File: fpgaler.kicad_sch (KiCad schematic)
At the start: 21 parts, among them J3 USB_C_Receptacle_USB2.0, J4 MicroSd, J5 JST

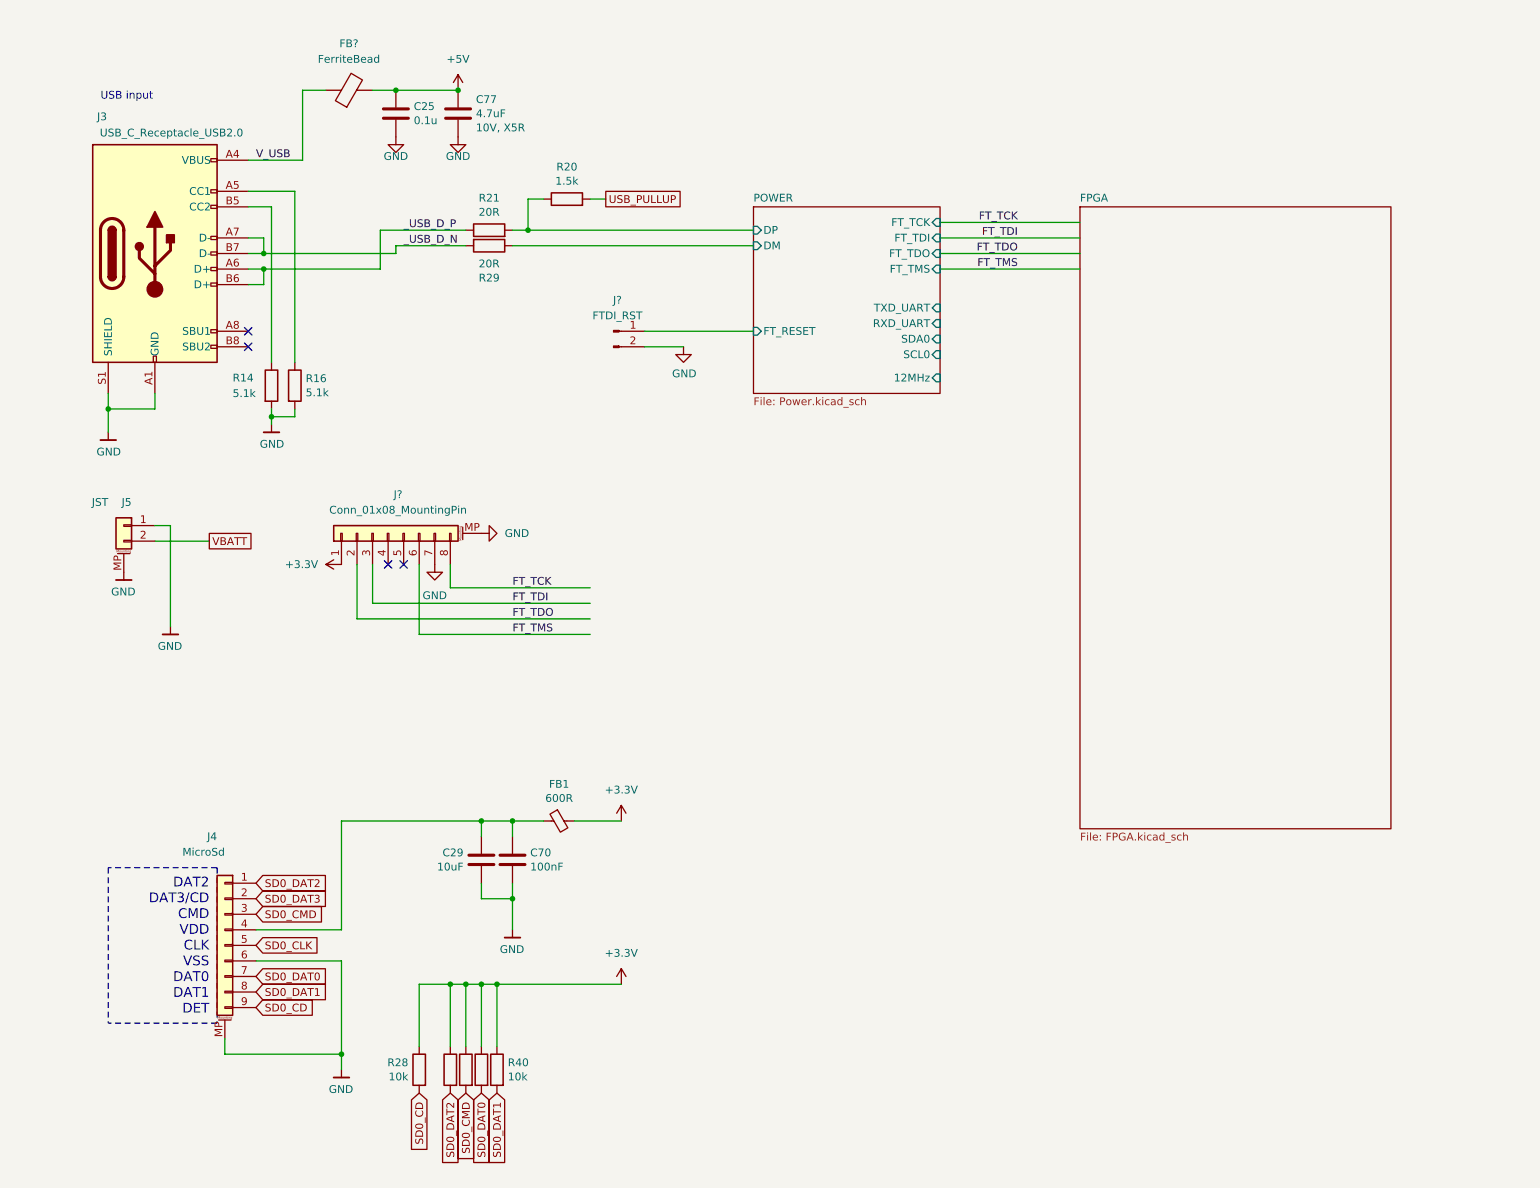
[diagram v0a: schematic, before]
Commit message: split fpga into two sheet. Connect jtag signals.
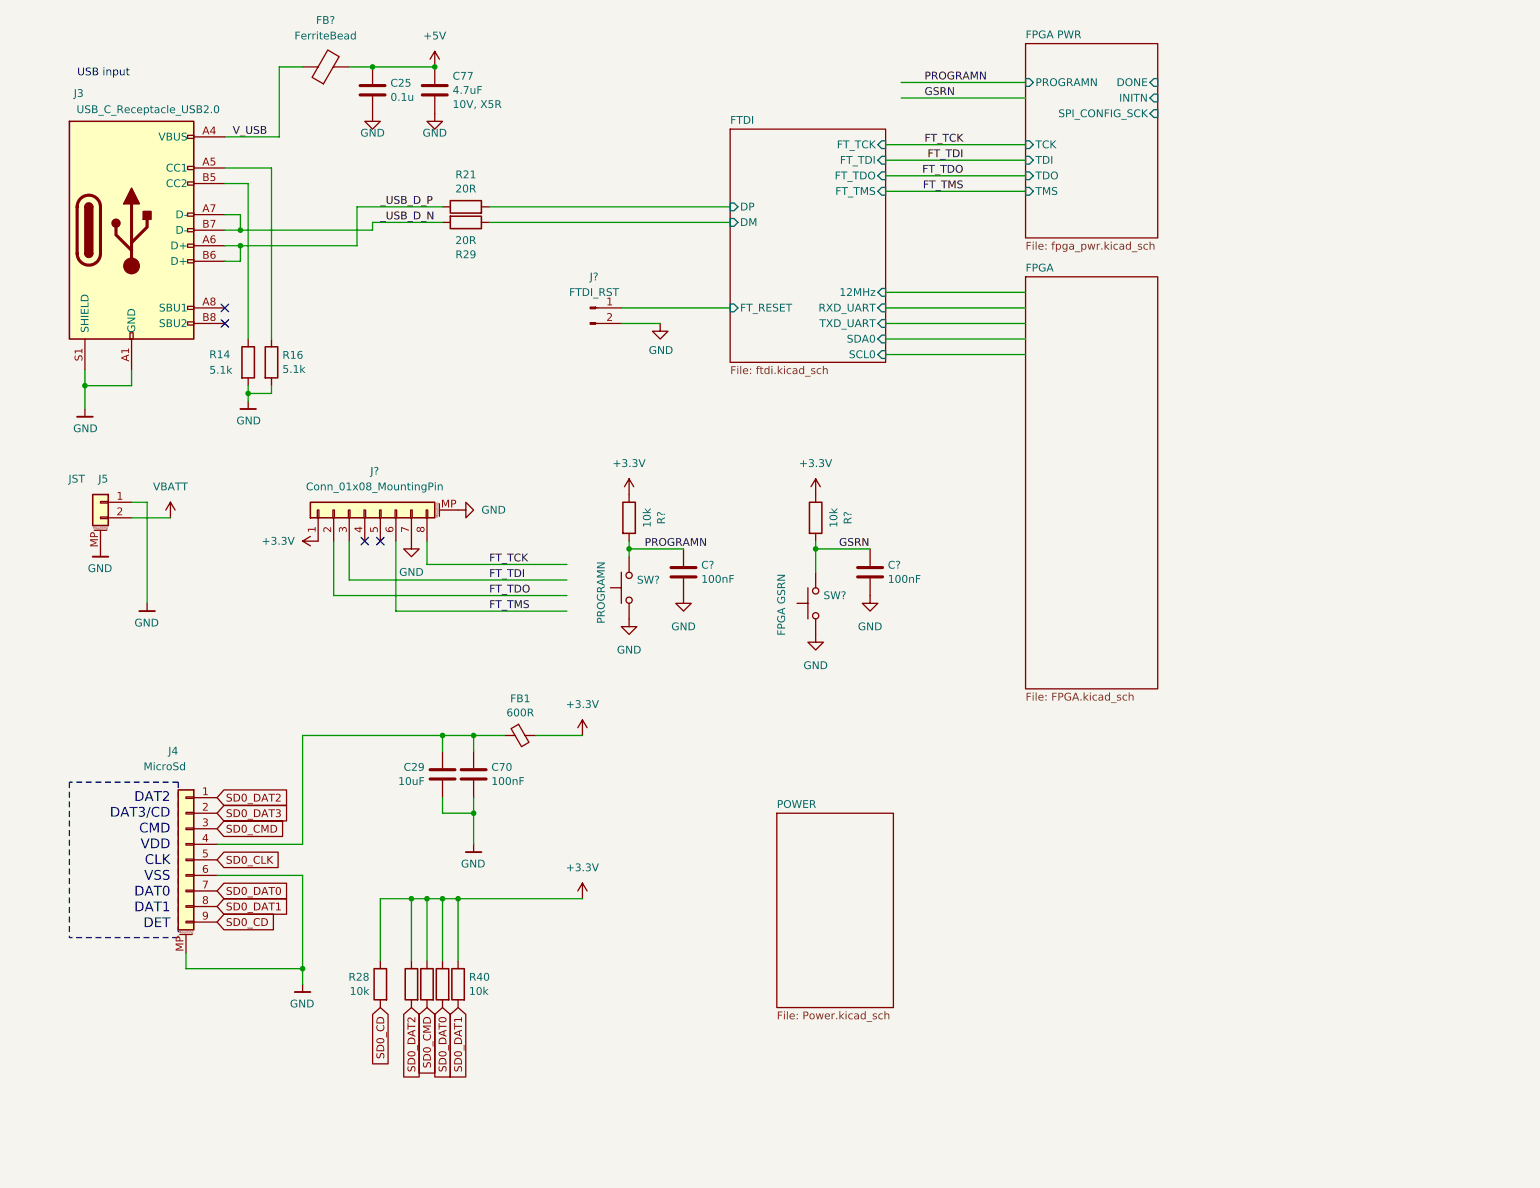
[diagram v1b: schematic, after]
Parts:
- removed R20: 1.5k, gkl_dipol:R_0201_0603Metric, symbol Device:R
- added C? (x2): 100nF, gkl_dipol:C_0201_0603Metric, symbol Device:C
- added R? (x2): 10k, gkl_dipol:R_0201_0603Metric, symbol Device:R
- added SW?: PROGRAMN, symbol Switch:SW_Push
- added SW?: FPGA GSRN, symbol Switch:SW_Push
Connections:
- net +3.3V: now also R?.1, R?.1
- net GND: now also C?.1, C?.1, SW?.1, SW?.1
- net POWER/DM renamed FTDI/DM
- net POWER/DP renamed FTDI/DP
- net POWER/FT_RESET renamed FTDI/FT_RESET
- new net GSRN: C?.2, R?.2, SW?.2
- new net PROGRAMN: C?.2, R?.2, SW?.2
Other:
- added sheet FPGA PWR (fpga_pwr.kicad_sch)
- added sheet FTDI (ftdi.kicad_sch)
- sheet POWER ports: added none; removed 12MHz, DM, DP, FT_RESET, FT_TCK, FT_TDI, FT_TDO, FT_TMS, RXD_UART, SCL0, SDA0, TXD_UART
- title: (none) -> FPGALER 
- moved on the sheet: C25, C29, C70, C77, FB1, FB?, J3, J4, J5, J?, R14, R16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

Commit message: complete scheme, add rotary switch, leds and buttons
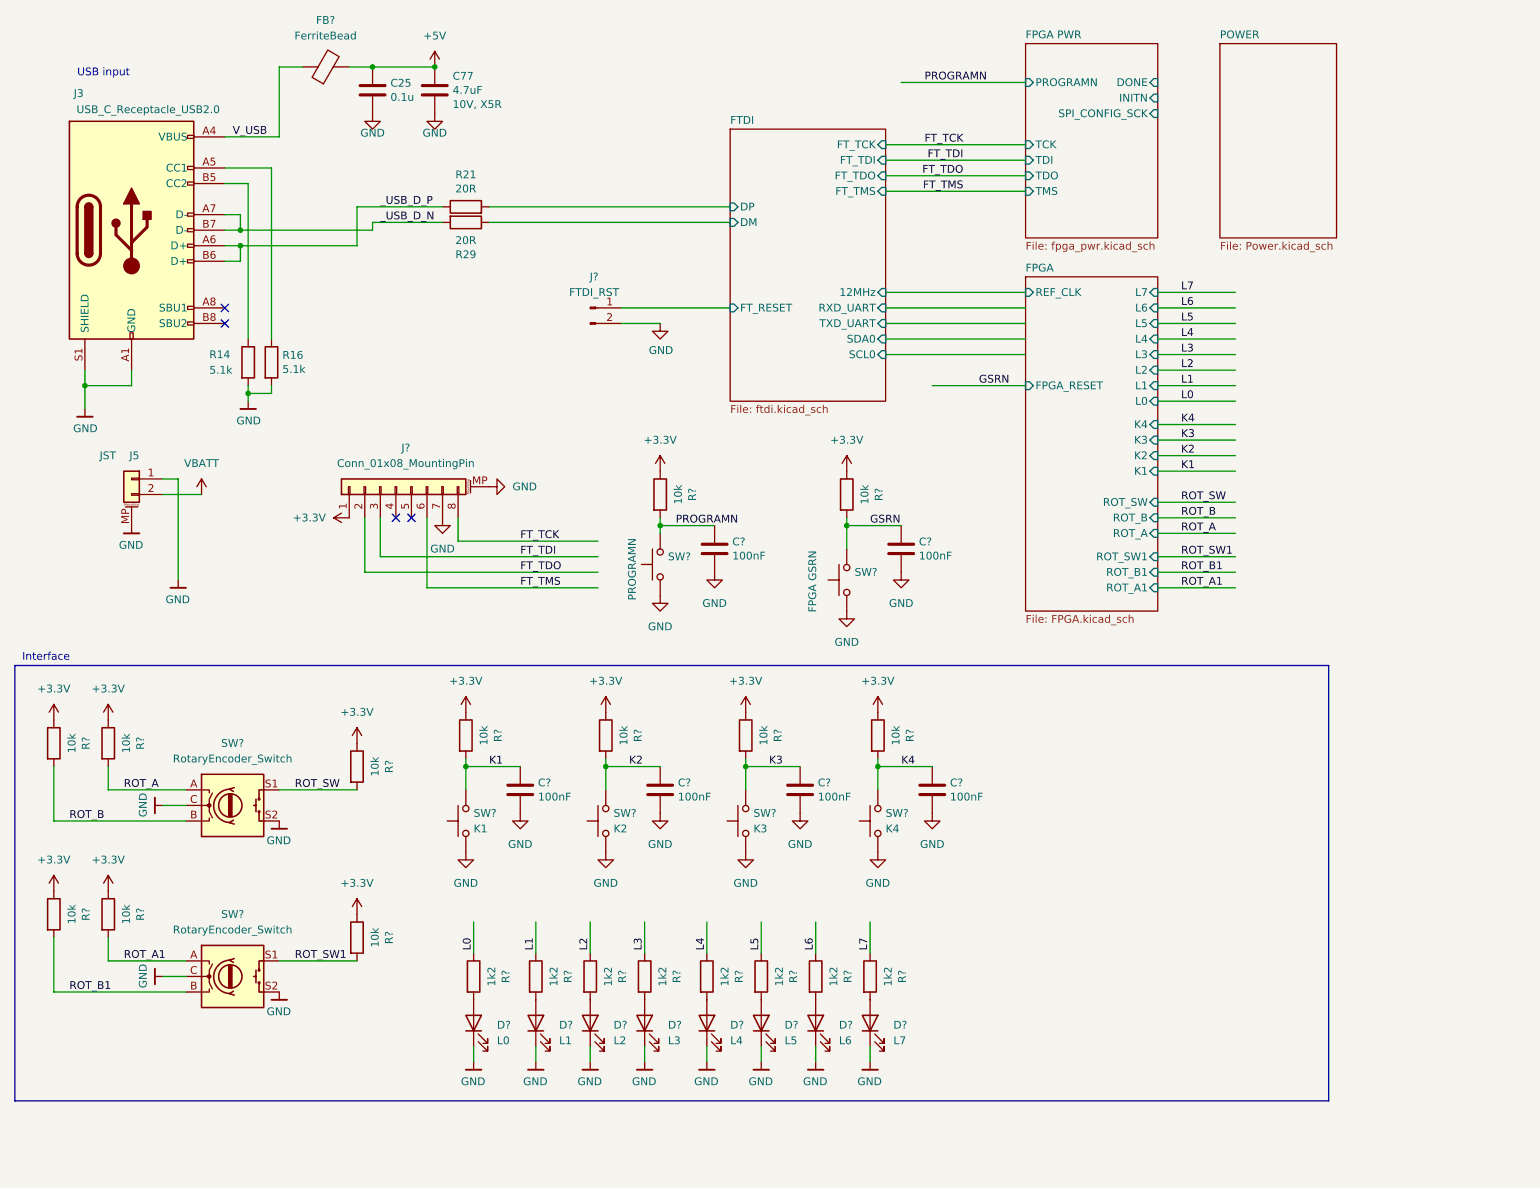
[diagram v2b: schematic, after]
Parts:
- removed C29: 10uF, Capacitor_SMD:C_0402_1005Metric, symbol Device:C
- removed C70: 100nF, gkl_dipol:C_0201_0603Metric, symbol Device:C
- removed FB1: 600R, Inductor_SMD:L_0402_1005Metric, symbol Device:Ferrite_Bead_Small
- removed J4: MicroSd, gkl_conn:molex_microsd_1040310811, symbol Connector_Generic_MountingPin:Conn_01x09_MountingPin
- removed R28, R40, R41, R42, R43: 10k, gkl_dipol:R_0201_0603Metric, symbol Device:R
- added C? (x4): 100nF, gkl_dipol:C_0201_0603Metric, symbol Device:C
- added D?: L3, symbol Device:LED
- added D?: L4, symbol Device:LED
- added D?: L0, symbol Device:LED
- added D?: L7, symbol Device:LED
- added D?: L6, symbol Device:LED
- added D?: L2, symbol Device:LED
- added D?: L1, symbol Device:LED
- added D?: L5, symbol Device:LED
- added R? (x10): 10k, gkl_dipol:R_0201_0603Metric, symbol Device:R
- added R? (x8): 1k2, gkl_dipol:R_0201_0603Metric, symbol Device:R
- added SW? (x2): RotaryEncoder_Switch, symbol Device:RotaryEncoder_Switch
- added SW?: K1, symbol Switch:SW_Push
- added SW?: K3, symbol Switch:SW_Push
- added SW?: K2, symbol Switch:SW_Push
- added SW?: K4, symbol Switch:SW_Push
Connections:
- net +3.3V: now also R?.1, R?.1, R?.1, R?.1, R?.1, R?.1, R?.1, R?.1, R?.1, R?.1
- net GND: now also C?.1, C?.1, C?.1, C?.1, D?.1 (K), D?.1 (K), D?.1 (K), D?.1 (K), D?.1 (K), D?.1 (K), D?.1 (K), D?.1 (K), SW?.1, SW?.1, SW?.1, SW?.1, SW?.C, SW?.C, SW?.S2, SW?.S2
- new net: D?.2 (A), R?.2 (x8)
- new net K1: C?.2, R?.2, SW?.2
- new net K2: C?.2, R?.2, SW?.2
- new net K3: C?.2, R?.2, SW?.2
- new net K4: C?.2, R?.2, SW?.2
- new net L0: R?.1
- new net L1: R?.1
- new net L2: R?.1
- new net L3: R?.1
- new net L4: R?.1
- new net L5: R?.1
- new net L6: R?.1
- new net L7: R?.1
- new net ROT_A: R?.2, SW?.A
- new net ROT_A1: R?.2, SW?.A
- new net ROT_B: R?.2, SW?.B
- new net ROT_B1: R?.2, SW?.B
- new net ROT_SW: R?.2, SW?.S1
- new net ROT_SW1: R?.2, SW?.S1
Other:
- sheet FPGA ports: added FPGA_RESET, K1, K2, K3, K4, L0, L1, L2, L3, L4, L5, L6, L7, REF_CLK, ROT_A, ROT_A1, ROT_B, ROT_B1, ROT_SW, ROT_SW1; removed none
- note added: "Interface"
- note removed: "DAT2 DAT3/CD CMD VDD CLK VSS DAT0 DAT1 DET"
- moved on the sheet: C?, J5, J?, R?, SW?

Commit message: start to assign footprint
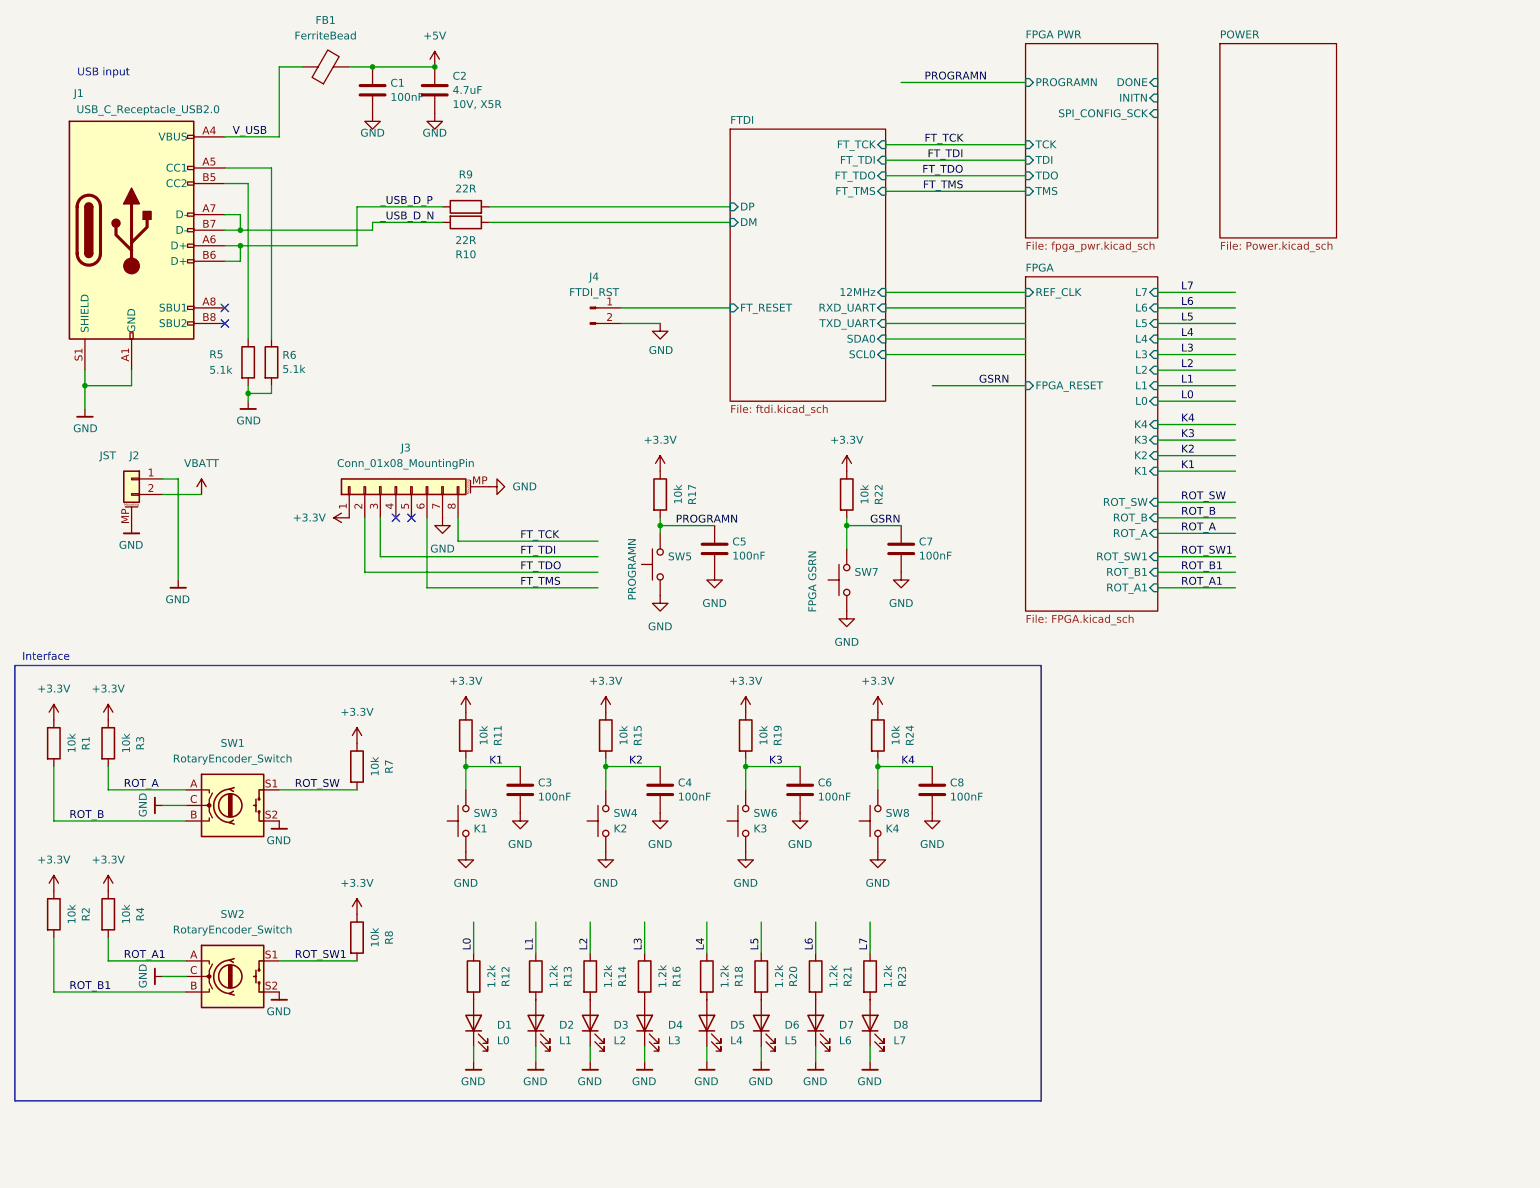
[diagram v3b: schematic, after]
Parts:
- C1: renamed from C25; value 0.1u -> 100nF
- C2: renamed from C77; footprint Capacitor_SMD:C_0402_1005Metric -> Capacitor_SMD:C_0805_2012Metric
- C3, C4, C5, C6, C7, C8: renamed from C?; footprint gkl_dipol:C_0201_0603Metric -> Capacitor_SMD:C_0603_1608Metric
- D1, D2, D3, D4, D5, D6, D7, D8: renamed from D?; footprint (none) -> Diode_SMD:D_0603_1608Metric
- J3: renamed from J?; footprint (none) -> Connector_PinHeader_2.54mm:PinHeader_1x08_P2.54mm_Vertical
- J4: renamed from J?; footprint (none) -> Connector_PinHeader_2.54mm:PinHeader_1x02_P2.54mm_Vertical
- R1, R11, R15, R17, R19, R2, R22, R24, R3, R4, R7, R8: renamed from R?; footprint gkl_dipol:R_0201_0603Metric -> Resistor_SMD:R_0603_1608Metric
- R10: renamed from R29; value 20R -> 22R; footprint gkl_dipol:R_0201_0603Metric -> Resistor_SMD:R_0603_1608Metric
- R12, R13, R14, R16, R18, R20, R21, R23: renamed from R?; value 1k2 -> 1.2k; footprint gkl_dipol:R_0201_0603Metric -> Resistor_SMD:R_0603_1608Metric
- R5: renamed from R14; footprint gkl_dipol:R_0201_0603Metric -> Resistor_SMD:R_0603_1608Metric
- R6: renamed from R16; footprint gkl_dipol:R_0201_0603Metric -> Resistor_SMD:R_0603_1608Metric
- R9: renamed from R21; value 20R -> 22R; footprint gkl_dipol:R_0201_0603Metric -> Resistor_SMD:R_0603_1608Metric
- SW1, SW2: renamed from SW?; footprint (none) -> Rotary_Encoder:RotaryEncoder_Alps_EC11E-Switch_Vertical_H20mm_CircularMountingHoles
- SW3, SW4, SW5, SW6, SW7, SW8: renamed from SW?; footprint (none) -> Button_Switch_THT:SW_PUSH_1P1T_6x3.5mm_H4.3_APEM_MJTP1243
- gave numbers to parts that had none: 1
- renumbered J3 to J1, J5 to J2
